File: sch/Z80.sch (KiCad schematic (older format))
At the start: 10 parts, among them IC1 Z80, IC10 74HC00, IC3 74HC541, IC4 74HC245, IC6 74HC541, IC9 74HC245

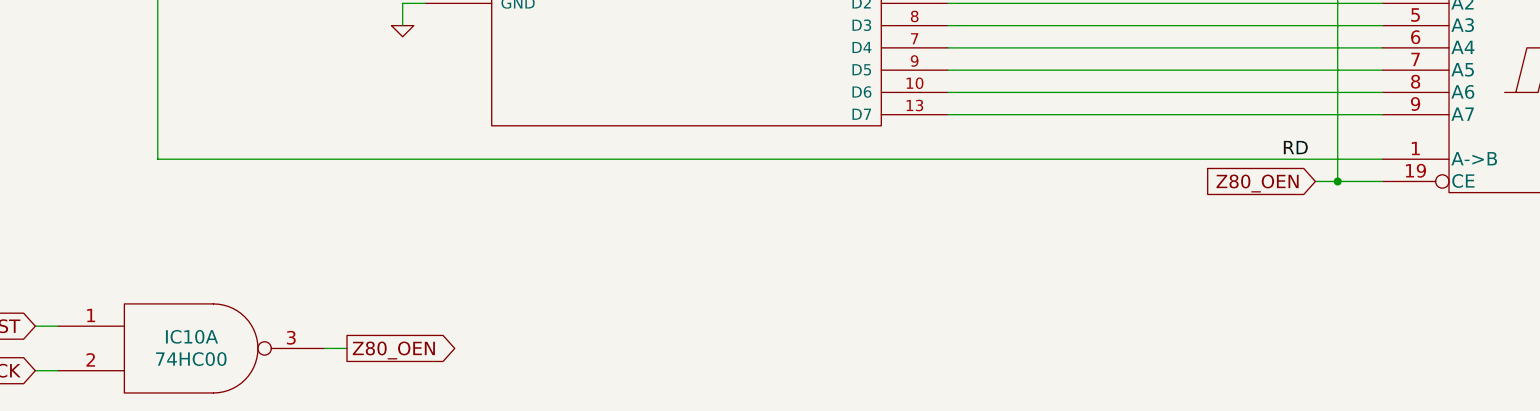
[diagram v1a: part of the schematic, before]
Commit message: Updated the code and circuit diagrams for first boot from banked RAM.
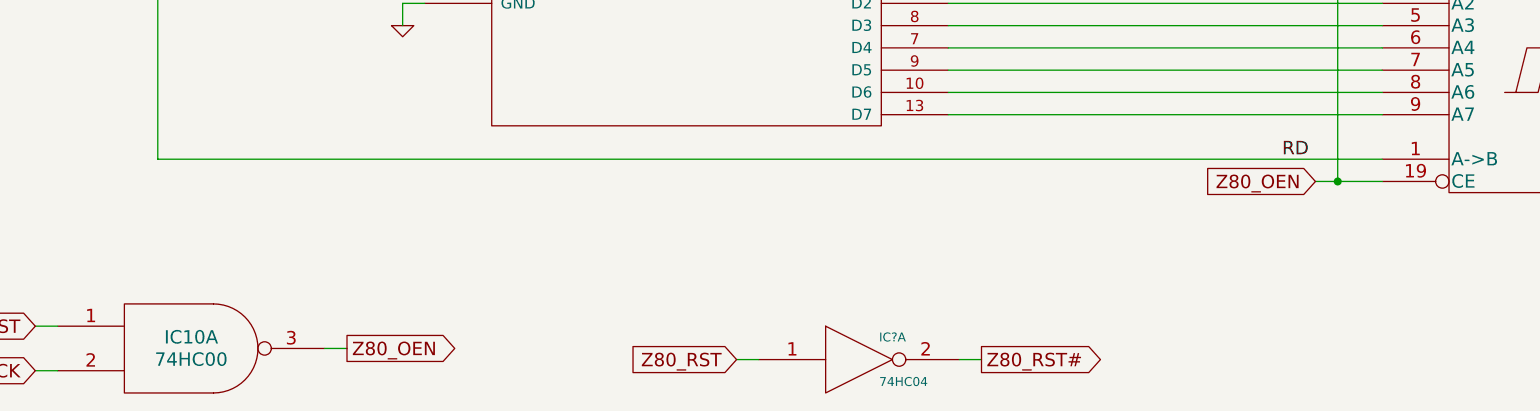
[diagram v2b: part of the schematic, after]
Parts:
- added IC?: 74HC04, 108-5299, symbol 74HC04
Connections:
- net GND: now also IC?.7 (GND)
- net VCC: now also IC?.14 (VCC)
- net Z80_RST: now also IC?.1
- new net Z80_RST#: IC?.2
